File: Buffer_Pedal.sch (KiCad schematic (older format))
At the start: 16 parts, among them J1 In, J2 Out, J3 9V, Q1 J113, Q2 J113

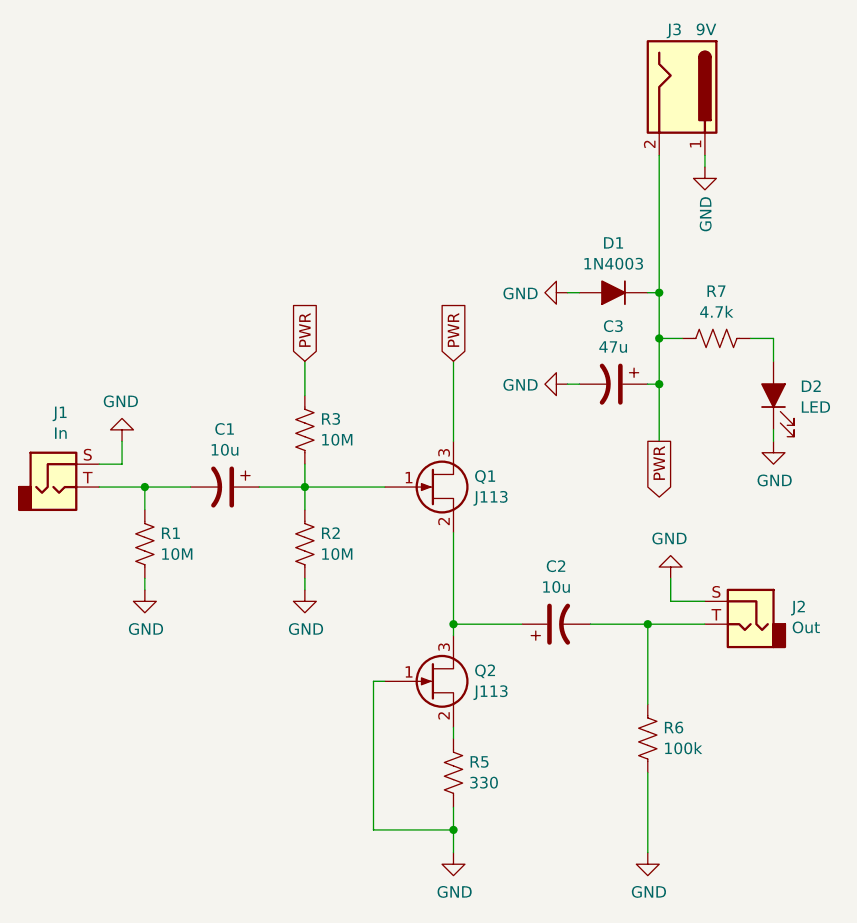
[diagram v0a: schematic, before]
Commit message: fixed JFET pinout
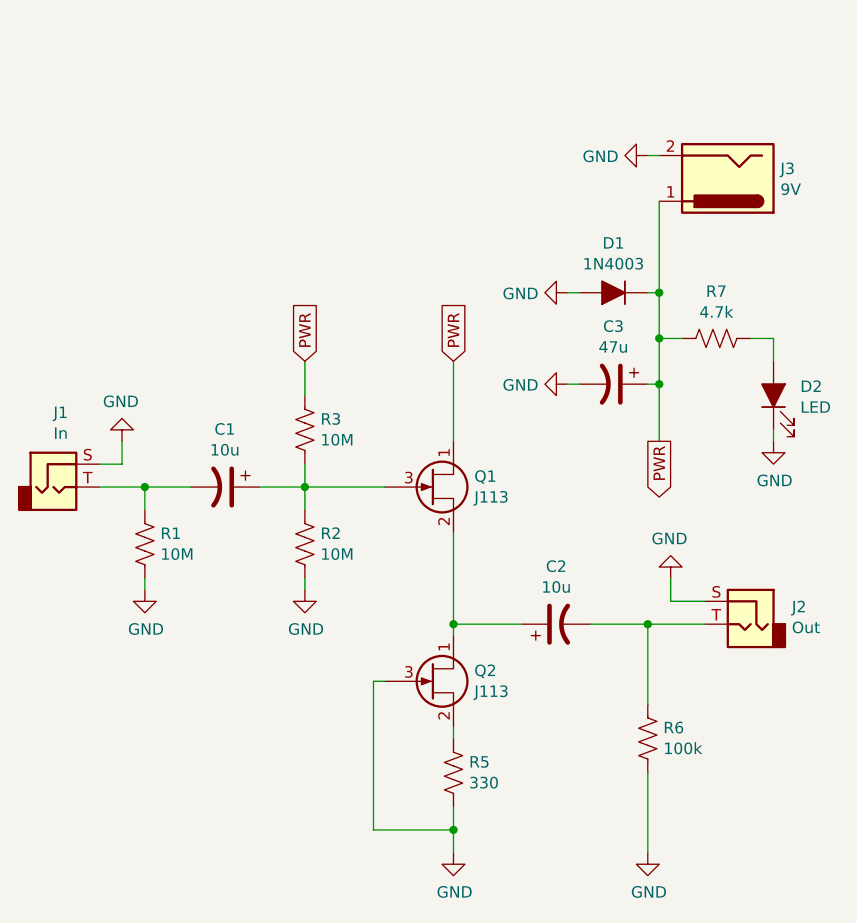
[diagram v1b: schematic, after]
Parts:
- removed Q1, Q2: J113, Package_TO_SOT_THT:TO-92, symbol Device:Q_NJFET_GSD
- added Q1, Q2: J113, Package_TO_SOT_THT:TO-92, symbol Device:Q_NJFET_DSG
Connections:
- net GND: now also J3.2, Q2.3 (G); no longer J3.1
- net PWR: now also J3.1, Q1.1 (D); no longer J3.2
- net at C1.1, R2.1, R3.2: now also Q1.3 (G)
- net at C2.1: now also Q1.2 (S), Q2.1 (D)
- net at R5.1: now also Q2.2 (S)
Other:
- moved on the sheet: J3
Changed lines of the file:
@@
 Wire Wire Line
 	4500 3600 4500 3750
-$Comp
-L Device:Q_NJFET_GSD Q1
-U 1 1 5DF3332A
-P 5050 4150
-F 0 "Q1" H 5241 4196 50  0000 L CNN
-F 1 "J113" H 5241 4105 50  0000 L CNN
-F 2 "Package_TO_SOT_THT:TO-92" H 5250 4250 50  0001 C CNN
-F 3 "~" H 5050 4150 50  0001 C CNN
-	1    5050 4150
-	1    0    0    -1
-$EndComp
 Wire Wire Line
 	4500 4150 4850 4150
@@
 Wire Wire Line
 	5150 3600 5150 3950
-$Comp
-L Device:Q_NJFET_GSD Q2
-U 1 1 5DF371C6
-P 5050 5000
-F 0 "Q2" H 5241 5046 50  0000 L CNN
-F 1 "J113" H 5241 4955 50  0000 L CNN
-F 2 "Package_TO_SOT_THT:TO-92" H 5250 5100 50  0001 C CNN
-F 3 "~" H 5050 5000 50  0001 C CNN
-	1    5050 5000
-	1    0    0    -1
-$EndComp
 $Comp
 L Device:R_US R5
@@
 	0    1    1    0
 $EndComp
+Connection ~ 6050 3300
 Wire Wire Line
 	6050 3300 6000 3300
@@
 	-1   0    0    1
 $EndComp
+Wire Wire Line
+	6050 2900 6050 3300
 $Comp
 L power:GND #PWR0110
 U 1 1 5DF924C2
-P 6250 2750
-F 0 "#PWR0110" H 6250 2500 50  0001 C CNN
-F 1 "GND" V 6255 2622 50  0000 R CNN
-F 2 "" H 6250 2750 50  0001 C CNN
-F 3 "" H 6250 2750 50  0001 C CNN
-	1    6250 2750
-	1    0    0    -1
-$EndComp
+P 6000 2700
+F 0 "#PWR0110" H 6000 2450 50  0001 C CNN
+F 1 "GND" V 6005 2572 50  0000 R CNN
+F 2 "" H 6000 2700 50  0001 C CNN
+F 3 "" H 6000 2700 50  0001 C CNN
+	1    6000 2700
+	0    1    1    0
+$EndComp
+Wire Wire Line
+	6000 2700 6050 2700
 $Comp
 L Connector:Barrel_Jack J3
 U 1 1 5DF8E3BD
-P 6150 2400
-F 0 "J3" V 5900 2400 50  0000 R CNN
-F 1 "9V" V 5900 2550 50  0000 R CNN
-F 2 "Connector_Wire:SolderWirePad_1x02_P3.81mm_Drill1.2mm" H 6200 2360 50  0001 C CNN
-F 3 "~" H 6200 2360 50  0001 C CNN
-	1    6150 2400
-	0    1    1    0
+P 6350 2800
+F 0 "J3" H 6120 2758 50  0000 R CNN
+F 1 "9V" H 6120 2849 50  0000 R CNN
+F 2 "Connector_Wire:SolderWirePad_1x02_P3.81mm_Drill1.2mm" H 6400 2760 50  0001 C CNN
+F 3 "~" H 6400 2760 50  0001 C CNN
+	1    6350 2800
+	-1   0    0    1
 $EndComp
 $Comp
@@
 Wire Wire Line
 	5150 4350 5150 4750
-Wire Wire Line
-	6050 2700 6050 3300
-Connection ~ 6050 3300
-Wire Wire Line
-	6250 2750 6250 2700
+$Comp
+L Device:Q_NJFET_DSG Q1
+U 1 1 5E0CCD01
+P 5050 4150
+F 0 "Q1" H 5241 4196 50  0000 L CNN
+F 1 "J113" H 5241 4105 50  0000 L CNN
+F 2 "Package_TO_SOT_THT:TO-92" H 5250 4250 50  0001 C CNN
+F 3 "~" H 5050 4150 50  0001 C CNN
+	1    5050 4150
+	1    0    0    -1
+$EndComp
+$Comp
+L Device:Q_NJFET_DSG Q2
+U 1 1 5E0CD1F9
+P 5050 5000
+F 0 "Q2" H 5241 5046 50  0000 L CNN
+F 1 "J113" H 5241 4955 50  0000 L CNN
+F 2 "Package_TO_SOT_THT:TO-92" H 5250 5100 50  0001 C CNN
+F 3 "~" H 5050 5000 50  0001 C CNN
+	1    5050 5000
+	1    0    0    -1
+$EndComp
 $EndSCHEMATC

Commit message: updated schematic and layout
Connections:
- net GND: now also J3.1; no longer J3.2
- net PWR: now also J3.2; no longer J3.1
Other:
- moved on the sheet: J3
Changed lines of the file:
@@
 Title "JFET Buffer"
 Date "2019-12-12"
-Rev "1"
+Rev "1.1"
 Comp "Chris Whitfill"
 Comment1 ""
@@
 	-1   0    0    1
 $EndComp
-Wire Wire Line
-	6050 2900 6050 3300
 $Comp
 L power:GND #PWR0110
 U 1 1 5DF924C2
-P 6000 2700
-F 0 "#PWR0110" H 6000 2450 50  0001 C CNN
-F 1 "GND" V 6005 2572 50  0000 R CNN
-F 2 "" H 6000 2700 50  0001 C CNN
-F 3 "" H 6000 2700 50  0001 C CNN
-	1    6000 2700
-	0    1    1    0
-$EndComp
-Wire Wire Line
-	6000 2700 6050 2700
+P 6250 2900
+F 0 "#PWR0110" H 6250 2650 50  0001 C CNN
+F 1 "GND" V 6255 2772 50  0000 R CNN
+F 2 "" H 6250 2900 50  0001 C CNN
+F 3 "" H 6250 2900 50  0001 C CNN
+	1    6250 2900
+	1    0    0    -1
+$EndComp
+Wire Wire Line
+	6250 2900 6250 2850
 $Comp
 L Connector:Barrel_Jack J3
 U 1 1 5DF8E3BD
-P 6350 2800
-F 0 "J3" H 6120 2758 50  0000 R CNN
-F 1 "9V" H 6120 2849 50  0000 R CNN
-F 2 "Connector_Wire:SolderWirePad_1x02_P3.81mm_Drill1.2mm" H 6400 2760 50  0001 C CNN
-F 3 "~" H 6400 2760 50  0001 C CNN
-	1    6350 2800
-	-1   0    0    1
+P 6150 2550
+F 0 "J3" H 5920 2508 50  0000 R CNN
+F 1 "9V" H 5920 2599 50  0000 R CNN
+F 2 "Connector_Wire:SolderWirePad_1x02_P3.81mm_Drill1.2mm" H 6200 2510 50  0001 C CNN
+F 3 "~" H 6200 2510 50  0001 C CNN
+	1    6150 2550
+	0    1    1    0
 $EndComp
 $Comp
@@
 	1    0    0    -1
 $EndComp
+Wire Wire Line
+	6050 2850 6050 3300
 $EndSCHEMATC
